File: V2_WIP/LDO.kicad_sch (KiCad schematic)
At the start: 4 parts, among them U103 ICM-45686

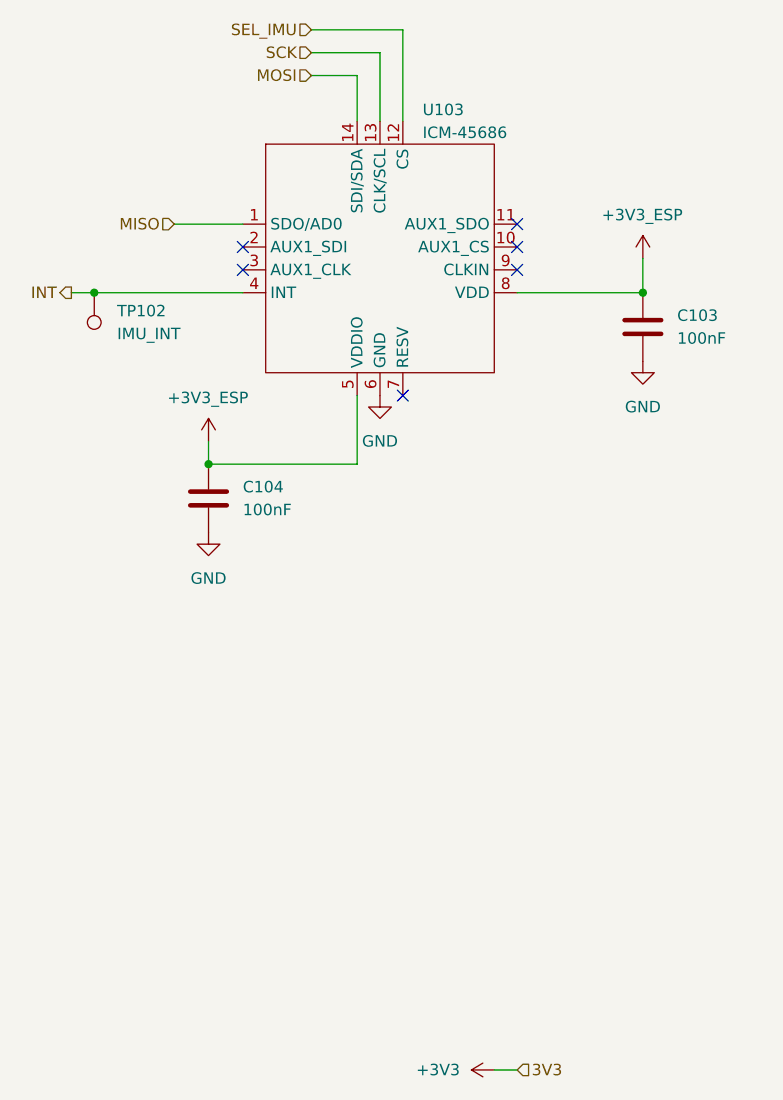
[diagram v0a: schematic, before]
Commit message: added second LDO
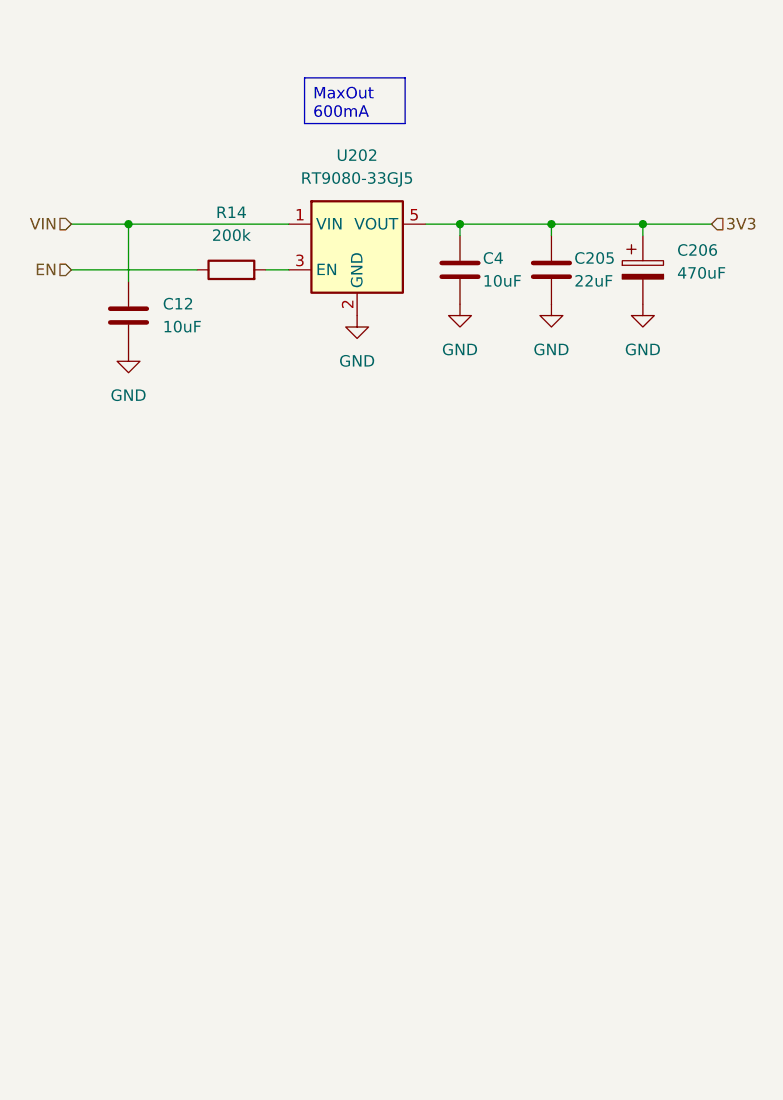
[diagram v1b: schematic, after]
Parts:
- removed C103, C104: 100nF, Capacitor_SMD:C_0603_1608Metric_Pad1.08x0.95mm_HandSolder, symbol Device:C
- removed TP102: IMU_INT, TestPoint:TestPoint_Pad_D1.0mm, symbol Connector:TestPoint
- removed U103: ICM-45686, Package_LGA:LGA-14_3x2.5mm_P0.5mm_LayoutBorder3x4y, symbol icm-45686:ICM-45686
- added C12, C4: 10uF, Capacitor_SMD:C_0603_1608Metric_Pad1.08x0.95mm_HandSolder, symbol Device:C
- added C205: 22uF, Capacitor_SMD:C_0603_1608Metric_Pad1.08x0.95mm_HandSolder, symbol Device:C
- added C206: 470uF, Capacitor_SMD:C_Elec_6.3x7.7, symbol Device:C_Polarized
- added R14: 200k, Resistor_SMD:R_0603_1608Metric_Pad0.98x0.95mm_HandSolder, symbol Device:R
- added U202: RT9080-33GJ5, Package_TO_SOT_SMD:SOT-23-5_HandSoldering, symbol Regulator_Linear:NCP163ASN500T1G
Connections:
- net GND: now also C12.2, C205.2, C206.2, C4.2, U202.2 (GND)
- new net: R14.2, U202.3 (EN)
- new net 3V3: C205.1, C206.1, C4.1, U202.5 (VOUT)
- new net EN: R14.1
- new net VIN: C12.1, U202.1 (VIN)
- no-connect marks 6 -> 0

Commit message: adjusted elec capacitors
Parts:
- C206: now not fitted
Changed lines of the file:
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@@
 		(on_board yes)
 		(in_pos_files yes)
-		(dnp no)
+		(dnp yes)
 		(fields_autoplaced yes)
 		(property "Reference" "C206"
